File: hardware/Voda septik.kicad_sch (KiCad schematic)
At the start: 41 parts, among them J1 Napájení a 4-20mA senzory, J2 Screw_Terminal_01x09, J3 Display LCD I2C, J4 Display TM1637, U1 DC-DC 24V -> 5V, U2 MAX3485-modul, U3 ADS1115IDGS, U4 ESP32-DevKitC, U5 CA56-12CGKWA

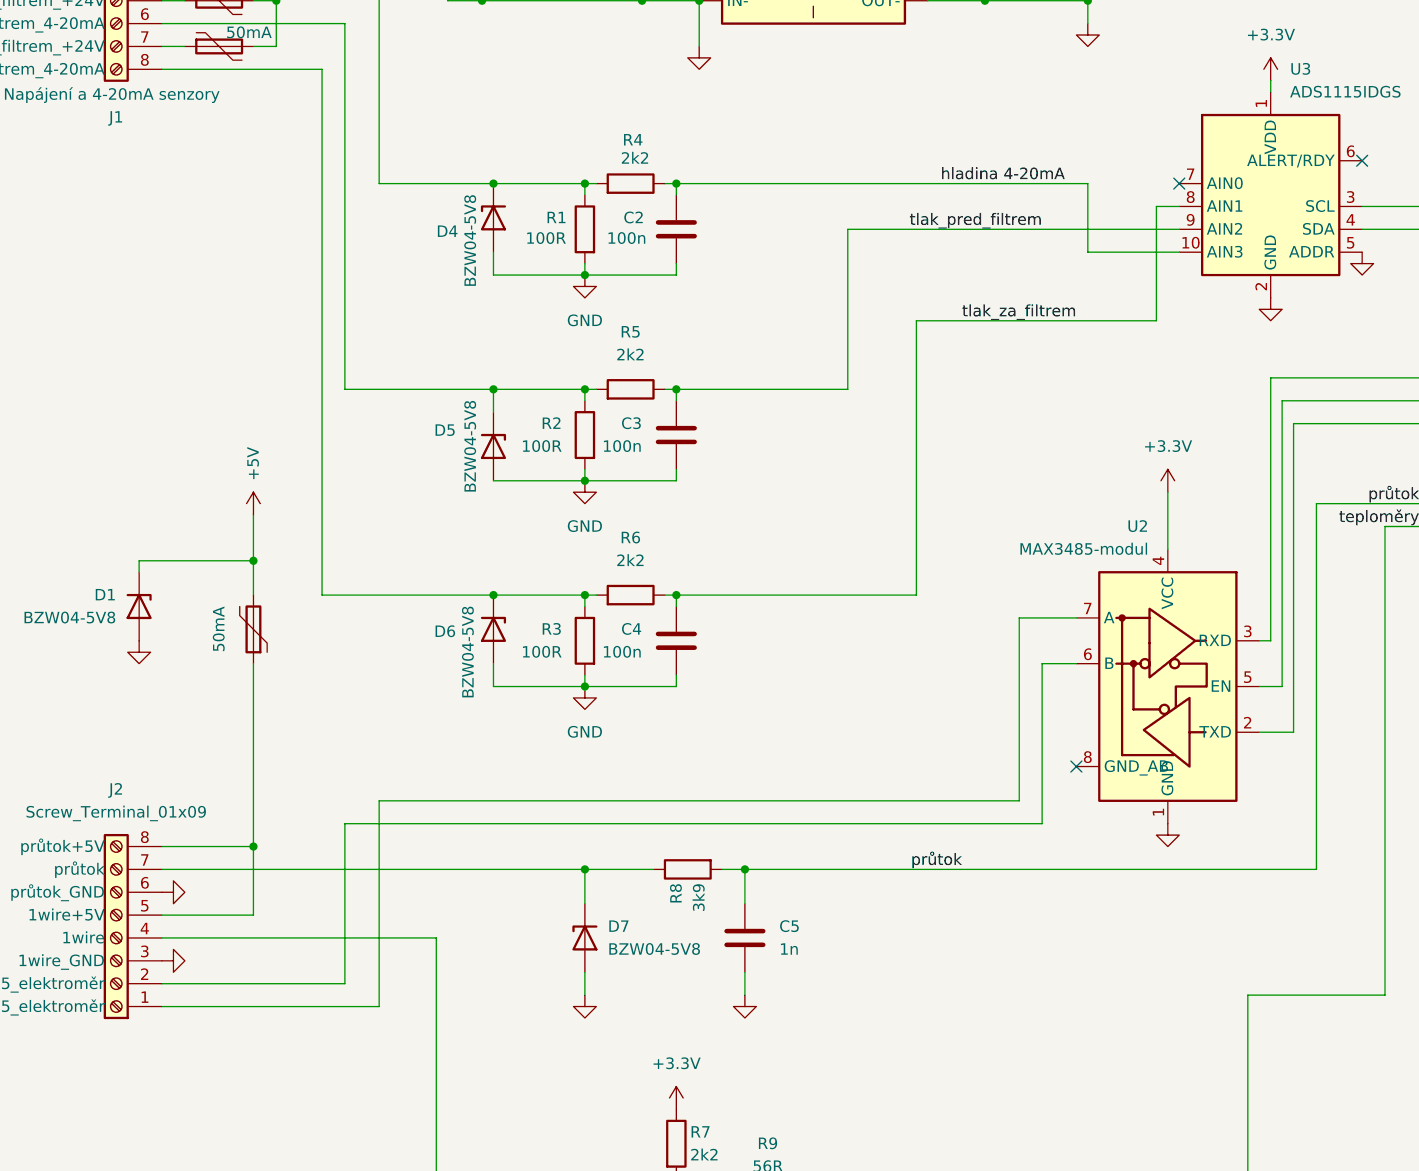
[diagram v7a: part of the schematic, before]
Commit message: Udělat hezčí schéma aby se tak nekřížily vývody
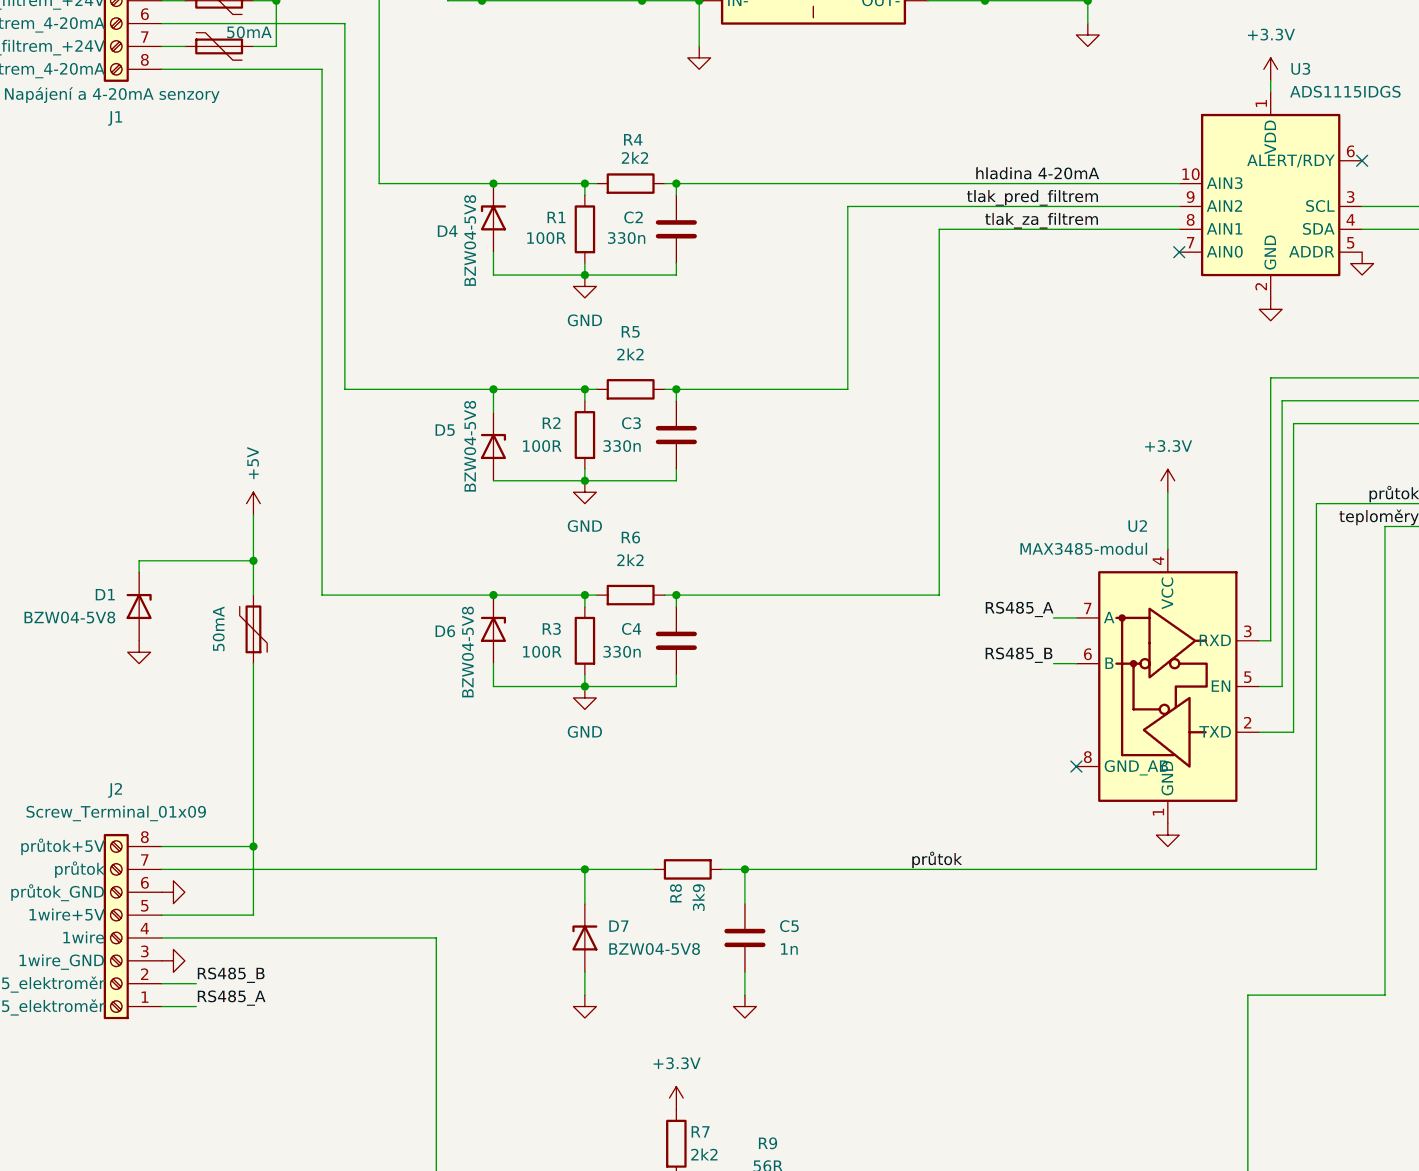
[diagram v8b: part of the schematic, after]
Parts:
- C2, C3, C4: value 100n -> 330n
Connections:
- net RS485_B: now reaches J2.2 (B_RS485_elektroměr), U2.6 (B)
- net RS485_A: now reaches J2.1 (A_RS485_elektroměr), U2.7 (A)
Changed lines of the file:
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@@
 	)
 	(no_connect
-		(at 158.75 53.34)
+		(at 158.75 60.96)
 	)
 	(no_connect
@@
 	(wire
 		(pts
-			(xy 102.87 99.06) (xy 129.54 99.06)
+			(xy 102.87 99.06) (xy 132.08 99.06)
 		)
 		(stroke
@@
 	(wire
 		(pts
-			(xy 66.04 142.24) (xy 45.72 142.24)
-		)
-		(stroke
-			(width 0)
-			(type default)
-		)
-	)
-	(wire
-		(pts
 			(xy 92.71 99.06) (xy 93.98 99.06)
 		)
@@
 	(wire
 		(pts
-			(xy 66.04 124.46) (xy 66.04 142.24)
-		)
-		(stroke
-			(width 0)
-			(type default)
-		)
-	)
-	(wire
-		(pts
 			(xy 82.55 99.06) (xy 92.71 99.06)
 		)
@@
 	(wire
 		(pts
-			(xy 66.04 124.46) (xy 143.51 124.46)
-		)
-		(stroke
-			(width 0)
-			(type default)
-		)
-	)
-	(wire
-		(pts
 			(xy 148.59 20.32) (xy 148.59 22.86)
 		)
@@
 		)
 	)
-	(wire
-		(pts
-			(xy 156.21 55.88) (xy 156.21 68.58)
-		)
-		(stroke
-			(width 0)
-			(type default)
-		)
-	)
 	(polyline
 		(pts
@@
 	(wire
 		(pts
-			(xy 129.54 99.06) (xy 129.54 68.58)
+			(xy 132.08 99.06) (xy 132.08 58.42)
 		)
 		(stroke
@@
 		)
 	)
-	(wire
-		(pts
-			(xy 143.51 124.46) (xy 143.51 106.68)
-		)
-		(stroke
-			(width 0)
-			(type default)
-		)
-	)
 	(polyline
 		(pts
@@
 	(wire
 		(pts
-			(xy 69.85 144.78) (xy 45.72 144.78)
-		)
-		(stroke
-			(width 0)
-			(type default)
-		)
-	)
-	(wire
-		(pts
 			(xy 102.87 99.06) (xy 102.87 100.33)
 		)
@@
 	(wire
 		(pts
-			(xy 129.54 68.58) (xy 156.21 68.58)
-		)
-		(stroke
-			(width 0)
-			(type default)
-		)
-	)
-	(wire
-		(pts
-			(xy 148.59 60.96) (xy 158.75 60.96)
+			(xy 132.08 58.42) (xy 158.75 58.42)
 		)
 		(stroke
@@
 		)
 	)
-	(wire
+	(polyline
 		(pts
-			(xy 69.85 121.92) (xy 69.85 144.78)
+			(xy 262.89 153.67) (xy 262.89 154.94)
 		)
 		(stroke
@@
 		)
 	)
-	(polyline
+	(wire
 		(pts
-			(xy 262.89 153.67) (xy 262.89 154.94)
+			(xy 144.78 106.68) (xy 147.32 106.68)
 		)
 		(stroke
@@
 	(wire
 		(pts
-			(xy 137.16 33.02) (xy 148.59 33.02)
+			(xy 45.72 144.78) (xy 49.53 144.78)
 		)
 		(stroke
@@
 	(wire
 		(pts
-			(xy 82.55 60.96) (xy 82.55 63.5)
+			(xy 137.16 33.02) (xy 148.59 33.02)
 		)
 		(stroke
@@
 	(wire
 		(pts
-			(xy 92.71 109.22) (xy 102.87 109.22)
+			(xy 82.55 60.96) (xy 82.55 63.5)
 		)
 		(stroke
@@
 	(wire
 		(pts
-			(xy 81.28 24.13) (xy 81.28 22.86)
+			(xy 92.71 109.22) (xy 102.87 109.22)
 		)
 		(stroke
@@
 	(wire
 		(pts
-			(xy 92.71 129.54) (xy 92.71 133.35)
+			(xy 81.28 24.13) (xy 81.28 22.86)
 		)
 		(stroke
@@
 	(wire
 		(pts
-			(xy 148.59 22.86) (xy 148.59 24.13)
+			(xy 92.71 129.54) (xy 92.71 133.35)
 		)
 		(stroke
@@
 	(wire
 		(pts
-			(xy 173.99 129.54) (xy 173.99 88.9)
+			(xy 148.59 22.86) (xy 148.59 24.13)
 		)
 		(stroke
@@
 	(wire
 		(pts
-			(xy 102.87 107.95) (xy 102.87 109.22)
+			(xy 173.99 129.54) (xy 173.99 88.9)
 		)
 		(stroke
@@
 	(wire
 		(pts
-			(xy 143.51 106.68) (xy 147.32 106.68)
+			(xy 102.87 107.95) (xy 102.87 109.22)
 		)
 		(stroke
@@
 		)
 	)
-	(wire
-		(pts
-			(xy 140.97 101.6) (xy 140.97 121.92)
-		)
-		(stroke
-			(width 0)
-			(type default)
-		)
-	)
 	(polyline
 		(pts
@@
 	(wire
 		(pts
-			(xy 121.92 58.42) (xy 158.75 58.42)
-		)
-		(stroke
-			(width 0)
-			(type default)
-		)
-	)
-	(wire
-		(pts
 			(xy 148.59 35.56) (xy 148.59 33.02)
 		)
@@
 	(wire
 		(pts
-			(xy 156.21 55.88) (xy 158.75 55.88)
+			(xy 121.92 55.88) (xy 158.75 55.88)
 		)
 		(stroke
@@
 	(wire
 		(pts
-			(xy 102.87 53.34) (xy 148.59 53.34)
+			(xy 102.87 53.34) (xy 158.75 53.34)
 		)
 		(stroke
@@
 	(wire
 		(pts
-			(xy 121.92 58.42) (xy 121.92 76.2)
+			(xy 121.92 55.88) (xy 121.92 76.2)
 		)
 		(stroke
@@
 	(wire
 		(pts
-			(xy 140.97 121.92) (xy 69.85 121.92)
+			(xy 45.72 142.24) (xy 49.53 142.24)
 		)
 		(stroke
@@
 	(wire
 		(pts
-			(xy 105.41 33.02) (xy 105.41 38.1)
+			(xy 144.78 101.6) (xy 147.32 101.6)
 		)
 		(stroke
@@
 	(wire
 		(pts
-			(xy 92.71 53.34) (xy 93.98 53.34)
+			(xy 105.41 33.02) (xy 105.41 38.1)
 		)
 		(stroke
@@
 	(wire
 		(pts
-			(xy 181.61 143.51) (xy 181.61 91.44)
+			(xy 92.71 53.34) (xy 93.98 53.34)
 		)
 		(stroke
@@
 	(wire
 		(pts
-			(xy 273.05 90.17) (xy 276.86 90.17)
+			(xy 181.61 143.51) (xy 181.61 91.44)
 		)
 		(stroke
@@
 	(wire
 		(pts
-			(xy 260.35 69.85) (xy 260.35 77.47)
+			(xy 273.05 90.17) (xy 276.86 90.17)
 		)
 		(stroke
@@
 	(wire
 		(pts
-			(xy 55.88 33.02) (xy 58.42 33.02)
+			(xy 260.35 69.85) (xy 260.35 77.47)
 		)
 		(stroke
@@
 	(wire
 		(pts
-			(xy 166.37 166.37) (xy 166.37 143.51)
+			(xy 55.88 33.02) (xy 58.42 33.02)
 		)
 		(stroke
@@
 	(wire
 		(pts
-			(xy 148.59 53.34) (xy 148.59 60.96)
+			(xy 166.37 166.37) (xy 166.37 143.51)
 		)
 		(stroke
@@
 	(wire
 		(pts
-			(xy 140.97 101.6) (xy 147.32 101.6)
-		)
-		(stroke
-			(width 0)
-			(type default)
-		)
-	)
-	(wire
-		(pts
 			(xy 55.88 106.68) (xy 55.88 127)
 		)
@@
 	)
 	(label "tlak_za_filtrem"
-		(at 147.32 68.58 180)
+		(at 149.86 58.42 180)
 		(effects
 			(font
@@
 	)
 	(label "tlak_pred_filtrem"
-		(at 143.51 58.42 180)
+		(at 149.86 55.88 180)
 		(effects
 			(font
@@
 		)
 	)
+	(label "RS485_B"
+		(at 144.78 106.68 180)
+		(effects
+			(font
+				(size 1.27 1.27)
+			)
+			(justify right bottom)
+		)
+	)
+	(label "RS485_B"
+		(at 49.53 142.24 0)
+		(effects
+			(font
+				(size 1.27 1.27)
+			)
+			(justify left bottom)
+		)
+	)
+	(label "RS485_A"
+		(at 144.78 101.6 180)
+		(effects
+			(font
+				(size 1.27 1.27)
+			)
+			(justify right bottom)
+		)
+	)
+	(label "RS485_A"
+		(at 49.53 144.78 0)
+		(effects
+			(font
+				(size 1.27 1.27)
+			)
+			(justify left bottom)
+		)
+	)
 	(label "hladina 4-20mA"
-		(at 146.05 53.34 180)
+		(at 149.86 53.34 180)
 		(effects
 			(font
@@
 			)
 		)
-		(property "Value" "100n"
+		(property "Value" "330n"
 			(at 99.06 105.4099 0)
 			(effects
@@
 			)
 		)
-		(property "Value" "100n"
+		(property "Value" "330n"
 			(at 99.06 82.5499 0)
 			(effects
@@
 			)
 		)
-		(property "Value" "100n"
+		(property "Value" "330n"
 			(at 99.568 59.436 0)
 			(effects
